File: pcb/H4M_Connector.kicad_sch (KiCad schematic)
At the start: 13 parts, among them J15 H4M_2x6_MDK

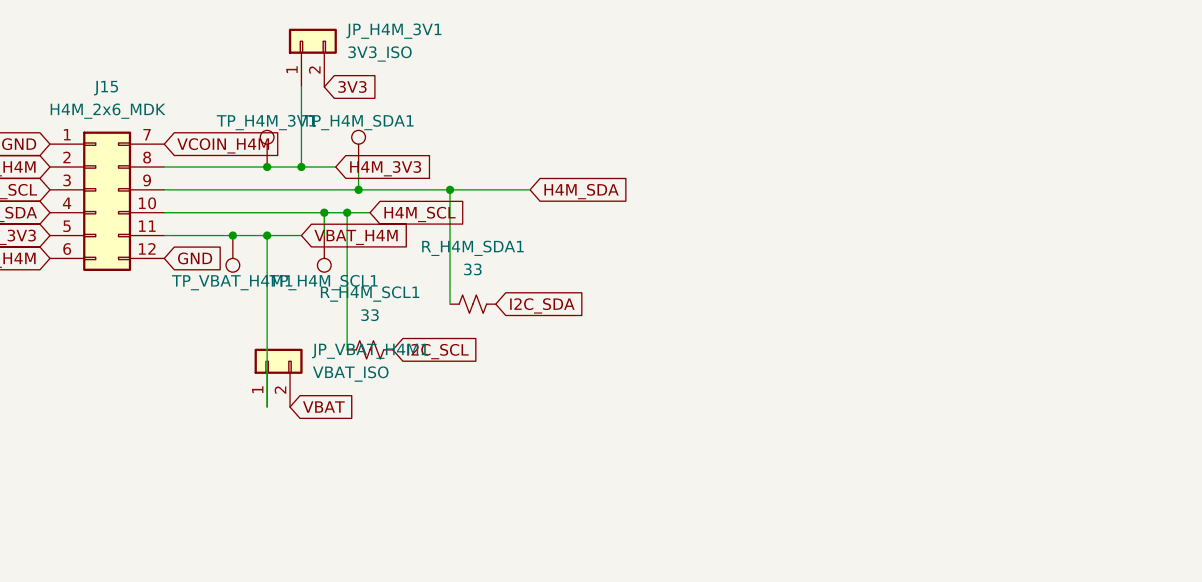
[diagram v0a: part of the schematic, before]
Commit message: solves no more direct-to-pin vias and routings
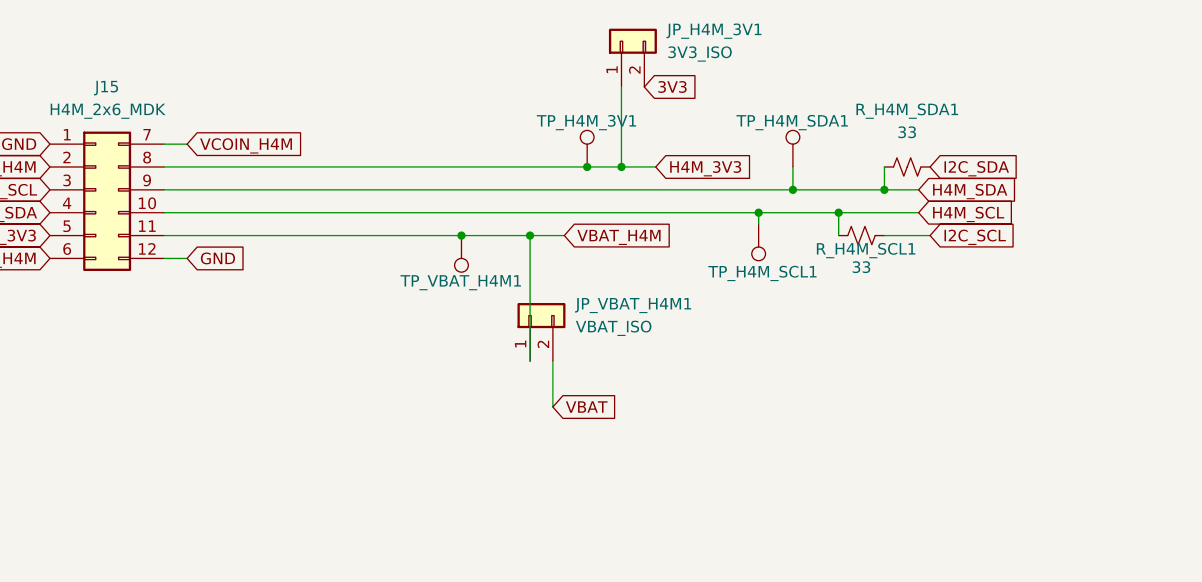
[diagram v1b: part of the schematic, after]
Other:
- moved on the sheet: JP_H4M_3V1, JP_VBAT_H4M1, R_H4M_SCL1, R_H4M_SDA1, TP_H4M_3V1, TP_H4M_SCL1, TP_H4M_SDA1, TP_VBAT_H4M1
